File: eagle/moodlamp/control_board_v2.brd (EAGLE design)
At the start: 49.5 x 43.2 mm, 38 parts, among them IC1 MEGA8-AI, J1 POWER_JACKPTH, Q1 N-HEXFET-2D_SOT232-IRLL014N, Q2 N-HEXFET-2D_SOT232-IRLL014N, Q3 N-HEXFET-2D_SOT232-IRLL014N

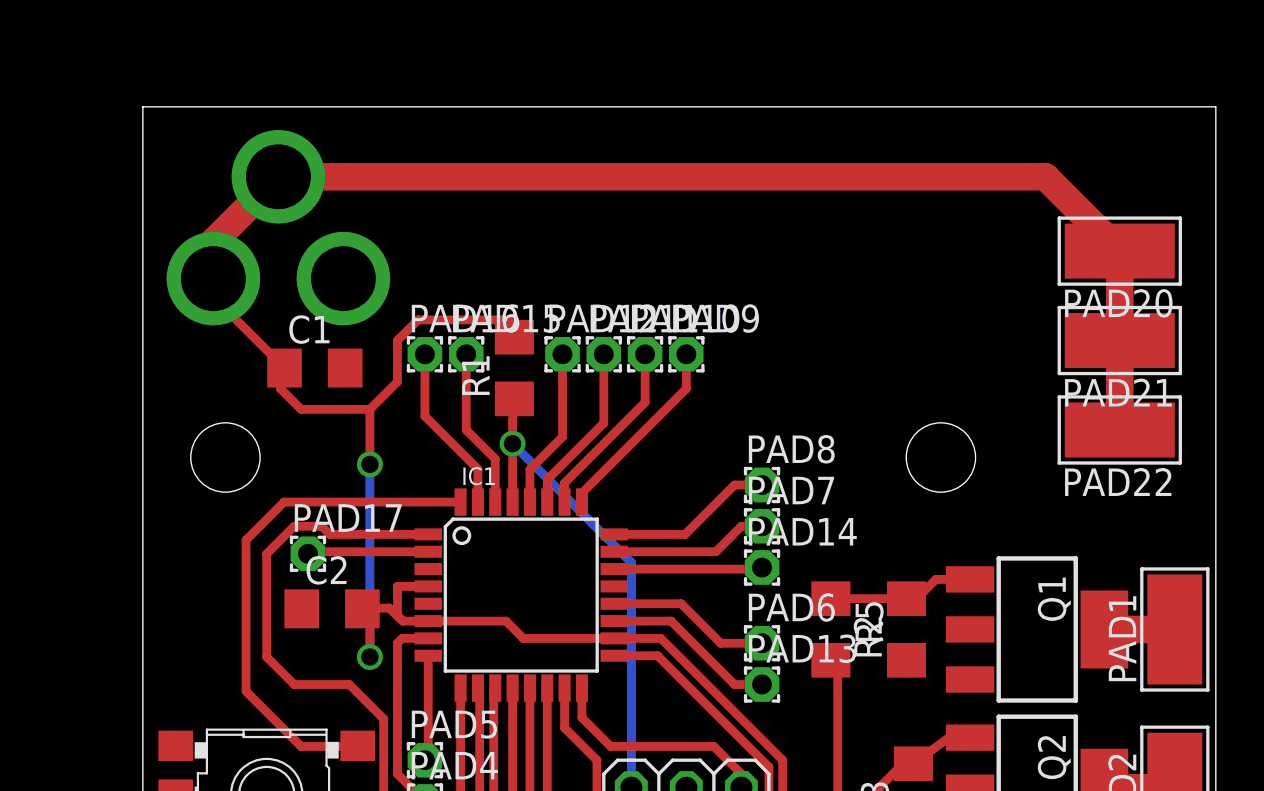
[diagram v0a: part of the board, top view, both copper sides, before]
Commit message: power jack fixed
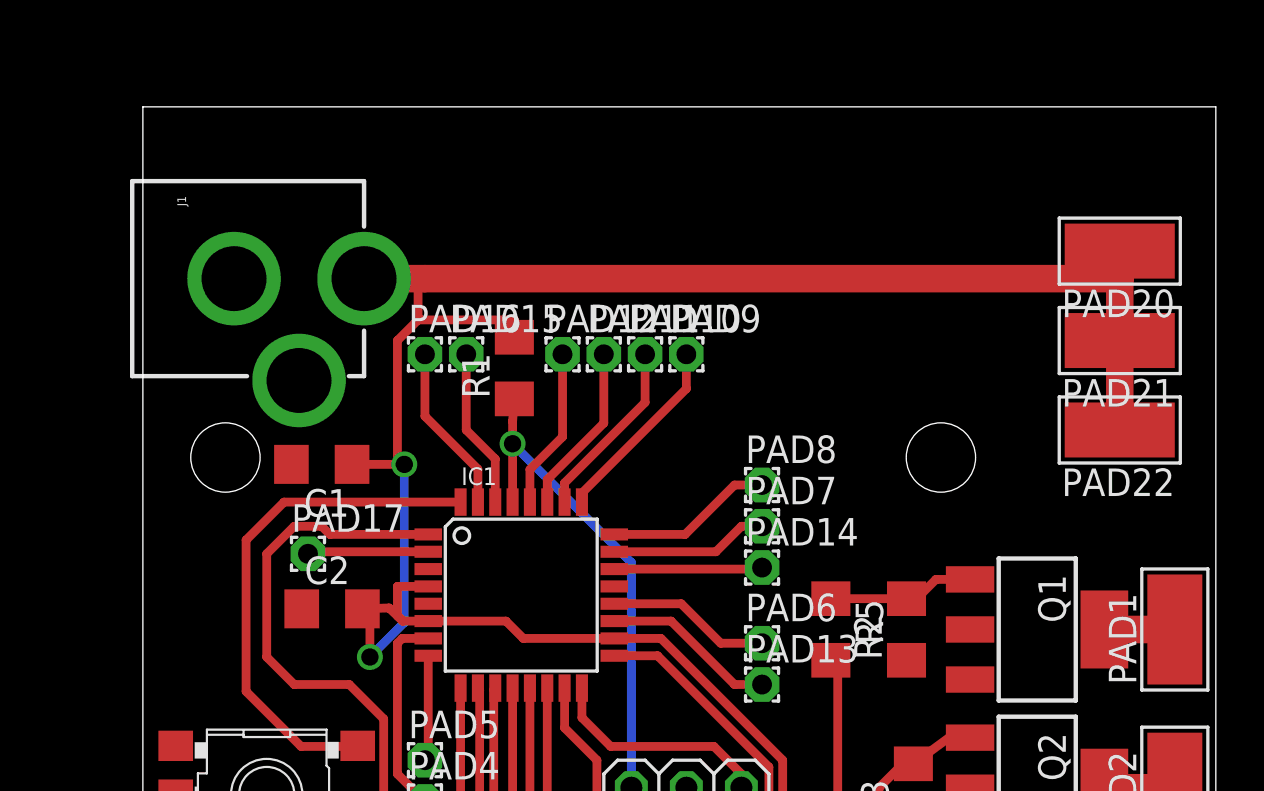
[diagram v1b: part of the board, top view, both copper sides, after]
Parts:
- moved C1 4.46 mm to (8.26, 26.7), turned to 180 degrees
- moved J1 0.95 mm to (-3.49, 35.2), flipped to the top, turned to 270 degrees
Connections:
- net GND: now also J1.GND, J1.GNDBREAK; no longer J1.PWR
- net VCC: now also J1.PWR; no longer J1.GND, J1.GNDBREAK
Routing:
- net VCC: track 120.0 -> 102.5 mm
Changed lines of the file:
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@@
 <attribute name="OC_FARNELL" value="9171371" x="47.9425" y="15.5575" size="1.778" layer="27" display="off"/>
 </element>
-<element name="J1" library="SparkFun" package="POWER_JACK_PTH" value="POWER_JACKPTH" x="-4.445" y="35.2425" rot="MR90"/>
-<element name="C1" library="resistor" package="C1206" value="" x="7.9375" y="31.115"/>
+<element name="J1" library="SparkFun" package="POWER_JACK_PTH" value="POWER_JACKPTH" x="-3.4925" y="35.2425" rot="R270"/>
+<element name="C1" library="resistor" package="C1206" value="" x="8.255" y="26.67" rot="R180"/>
 <element name="C2" library="resistor" package="C1206" value="" x="8.73125" y="20.0025"/>
 <element name="R1" library="resistor" package="R1206" value="" x="17.145" y="31.115" rot="R90"/>
@@
 <contactref element="IC1" pad="5"/>
 <contactref element="C1" pad="2"/>
-<contactref element="J1" pad="PWR"/>
 <contactref element="IC1" pad="21"/>
 <contactref element="Q1" pad="3"/>
@@
 <contactref element="USB1" pad="GND3"/>
 <contactref element="USB1" pad="GND4"/>
+<contactref element="J1" pad="GND"/>
+<contactref element="J1" pad="GNDBREAK"/>
 </signal>
 <signal name="VCC">
@@
 <contactref element="IC1" pad="4"/>
 <contactref element="C1" pad="1"/>
-<contactref element="J1" pad="GND"/>
-<contactref element="J1" pad="GNDBREAK"/>
 <contactref element="IC1" pad="18"/>
 <contactref element="R1" pad="2"/>
@@
 <contactref element="PAD21" pad="1"/>
 <contactref element="PAD22" pad="1"/>
-<wire x1="3.255" y1="35.2425" x2="3.255" y2="36.9425" width="1.27" layer="1"/>
-<wire x1="3.255" y1="36.9425" x2="6.255" y2="39.9425" width="1.27" layer="1"/>
-<wire x1="45.085" y1="36.5125" x2="41.655" y2="39.9425" width="1.27" layer="1"/>
-<wire x1="41.655" y1="39.9425" x2="6.255" y2="39.9425" width="1.27" layer="1"/>
-<wire x1="45.085" y1="36.5125" x2="45.085" y2="32.385" width="1.27" layer="1"/>
+<wire x1="45.085" y1="36.5125" x2="45.085" y2="35.2425" width="1.27" layer="1"/>
+<wire x1="45.085" y1="35.2425" x2="45.085" y2="32.385" width="1.27" layer="1"/>
 <wire x1="45.085" y1="32.385" x2="45.085" y2="28.2575" width="1.27" layer="1"/>
-<wire x1="3.255" y1="35.2425" x2="3.255" y2="34.3975" width="0.4064" layer="1"/>
-<wire x1="3.255" y1="34.3975" x2="6.5375" y2="31.115" width="0.4064" layer="1"/>
 <wire x1="21.7551" y1="18.6375" x2="17.5575" y2="18.6375" width="0.4064" layer="1"/>
 <wire x1="17.5575" y1="18.6375" x2="16.7575" y2="19.4375" width="0.4064" layer="1"/>
@@
 <wire x1="17.145" y1="33.3375" x2="12.7" y2="33.3375" width="0.4064" layer="1"/>
 <wire x1="12.7" y1="33.3375" x2="11.7475" y2="32.385" width="0.4064" layer="1"/>
-<wire x1="11.7475" y1="32.385" x2="11.7475" y2="30.48" width="0.4064" layer="1"/>
-<wire x1="10.4775" y1="29.21" x2="7.3025" y2="29.21" width="0.4064" layer="1"/>
-<wire x1="7.3025" y1="29.21" x2="6.35" y2="30.1625" width="0.4064" layer="1"/>
-<wire x1="6.35" y1="30.1625" x2="6.35" y2="30.9275" width="0.4064" layer="1"/>
-<wire x1="6.35" y1="30.9275" x2="6.5375" y2="31.115" width="0.4064" layer="1"/>
-<wire x1="10.4775" y1="29.21" x2="11.7475" y2="30.48" width="0.4064" layer="1"/>
-<wire x1="10.4775" y1="29.21" x2="10.4775" y2="26.67" width="0.4064" layer="1"/>
-<via x="10.4775" y="26.67" extent="1-16" drill="0.8"/>
-<wire x1="10.4775" y1="26.67" x2="10.4775" y2="17.78" width="0.4064" layer="16"/>
+<wire x1="11.7475" y1="32.385" x2="11.7475" y2="26.9875" width="0.4064" layer="1"/>
+<wire x1="11.7475" y1="26.9875" x2="12.065" y2="26.67" width="0.4064" layer="1"/>
+<via x="12.065" y="26.67" extent="1-16" drill="0.8"/>
+<wire x1="12.065" y1="26.67" x2="12.065" y2="19.3675" width="0.4064" layer="16"/>
+<wire x1="12.065" y1="19.3675" x2="10.4775" y2="17.78" width="0.4064" layer="16"/>
 <via x="10.4775" y="17.78" extent="1-16" drill="0.8"/>
 <wire x1="10.4775" y1="17.78" x2="10.4775" y2="19.65625" width="0.4064" layer="1"/>
 <wire x1="10.4775" y1="19.65625" x2="10.13125" y2="20.0025" width="0.4064" layer="1"/>
+<contactref element="J1" pad="PWR"/>
+<wire x1="10.2075" y1="35.2425" x2="13.0175" y2="35.2425" width="1.27" layer="1"/>
+<wire x1="13.0175" y1="35.2425" x2="45.085" y2="35.2425" width="1.27" layer="1"/>
+<wire x1="9.655" y1="26.67" x2="12.065" y2="26.67" width="0.4064" layer="1"/>
+<wire x1="12.7" y1="33.3375" x2="12.7" y2="35.2425" width="0.4064" layer="1"/>
+<wire x1="12.7" y1="35.2425" x2="13.0175" y2="35.2425" width="0.4064" layer="1"/>
 </signal>
 <signal name="RST">

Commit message: v2 prototype
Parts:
- added D1, D2: 3V6, diode:SOD80C
- added R6: 1k5, resistor:R0805
- added R7, R8: 68R, resistor:R0805
- C1, C2: device resistor:C1206 -> resistor:C0805
- PAD1, PAD2, PAD20, PAD21, PAD22, PAD3: value WIREPADSMD5-2,5 -> (none); device wirepad:5-2,5 -> wirepad:2,54/1,0
- R1, R2, R3, R4, R5: device resistor:R1206 -> resistor:R0805
- moved USB1 26.2 mm to (1.27, 23.2), turned to 0 degrees
- moved PAD17 20.5 mm to (18.4, 5.08)
- moved C1 11.8 mm to (15.6, 35.9), turned to 90 degrees
- moved PAD16 9.34 mm to (11.4, 22.5)
- moved PAD19 3.82 mm to (20.3, 5.08)
- moved C2 3.18 mm to (11.9, 20.0)
- moved PAD15 3.18 mm to (17.5, 29.8)
- moved JP1 2.88 mm to (27.9, 10.8)
- moved PAD10 2.69 mm to (25.1, 29.8)
- moved PAD12 2.69 mm to (21.3, 29.8)
- moved PAD9 2.69 mm to (27.0, 29.8)
- moved PAD11 2.69 mm to (23.2, 29.8)
- moved PAD4 2.62 mm to (15.6, 10.5)
- moved PAD5 2.62 mm to (15.6, 12.4)
- moved R1 2.56 mm to (19.4, 32.4)
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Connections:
- new net N$30: D1.C, R6.2, R7.2, USB1.2
- new net N$31: D2.C, R8.2, USB1.3
- net +5V: now also R6.1
- net GND: now also D1.A, D2.A
- net N$10: now also IC1.31, R7.1; no longer IC1.10, USB1.2
- net N$11: now also IC1.32, R8.1; no longer IC1.11, USB1.3
- net N$24: now also IC1.2; no longer IC1.31
- net N$25: now also IC1.11; no longer IC1.2
- net N$8: now also IC1.10, S2.3; no longer IC1.32, S1.3
- net N$9: now also S1.3; no longer S2.3
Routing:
- net N$30: track 0.00 -> 17.8 mm
- net N$9: track 28.7 -> 15.5 mm
- net N$10: track 12.0 -> 2.96 mm
- net VCC: track 102.5 -> 111.3 mm, vias 2 -> 0
- net +5V: track 0.00 -> 8.41 mm
- net N$31: track 0.00 -> 7.71 mm
- net N$11: track 12.0 -> 4.35 mm
- net N$8: track 23.8 -> 16.5 mm
- net GND: track 0.00 -> 6.30 mm, vias 0 -> 2
- net N$25: track 5.59 -> 11.3 mm
- net N$27: track 16.5 -> 11.7 mm
- net RST: track 22.9 -> 27.0 mm
- net N$24: track 7.83 -> 4.00 mm
- net N$12: track 7.50 -> 5.24 mm
- net N$6: track 31.4 -> 29.2 mm
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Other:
- board size 49.5 x 43.2 mm -> 49.5 x 40 mm
- board text added: "moodlamp v2"

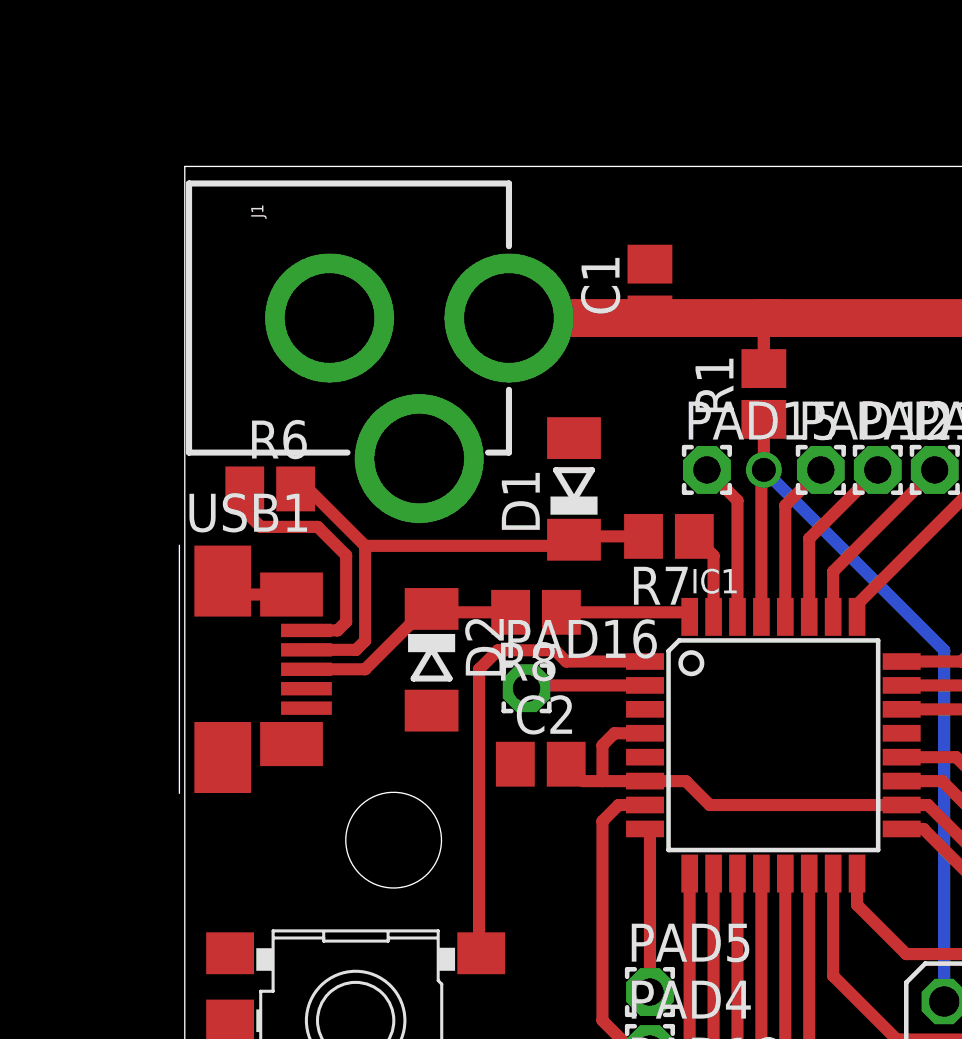
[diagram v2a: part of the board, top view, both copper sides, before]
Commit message: power jack orientation fixed
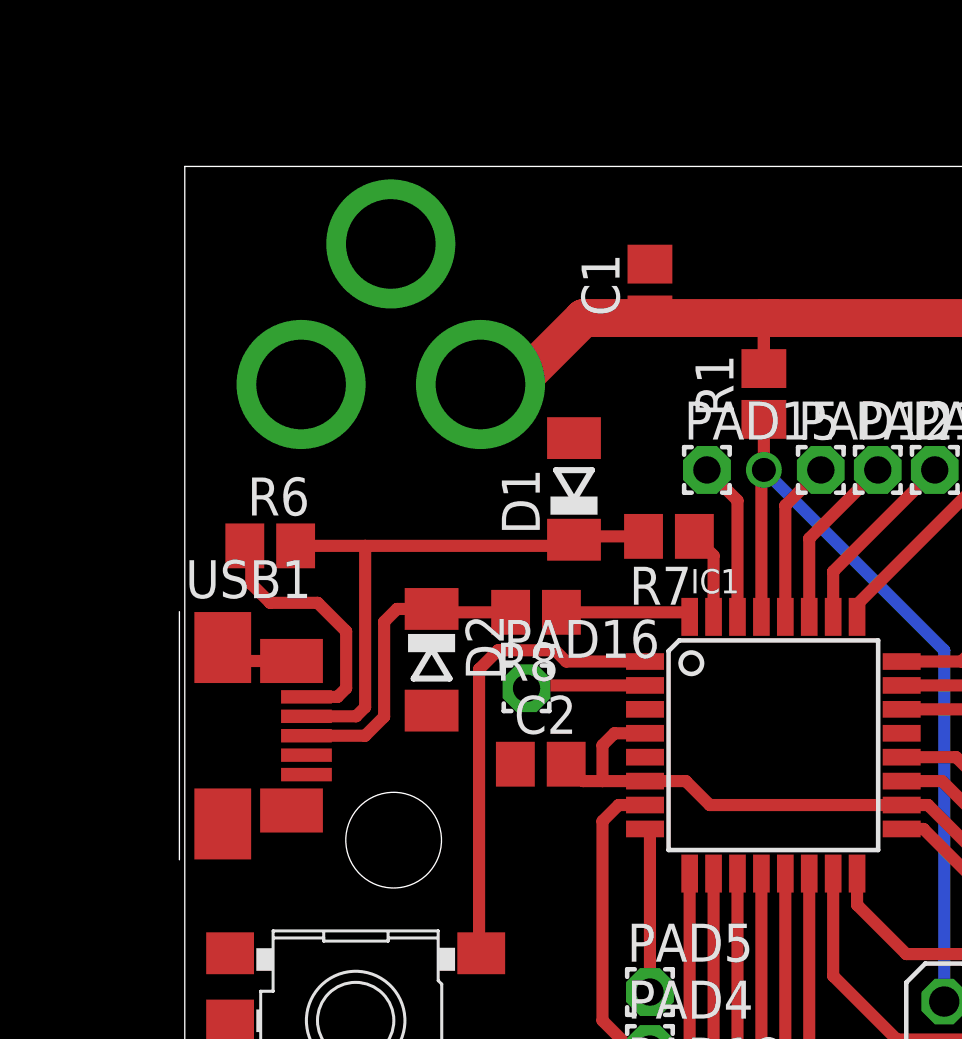
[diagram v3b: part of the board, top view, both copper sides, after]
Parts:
- moved J1 2.42 mm to (-3.81, 32.7), flipped to the bottom, turned to 90 degrees
- moved USB1 2.22 mm to (1.27, 21.0)
- moved R6 1.91 mm to (2.86, 27.3)
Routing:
- net N$31: track 7.71 -> 10.7 mm
- net VCC: track 111.3 -> 113.6 mm
- net N$30: track 17.8 -> 19.3 mm
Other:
- board text added: "tohle je moc blizko u sebe ->"
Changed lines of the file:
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@@
 <hole x="38.735" y="28.2575" drill="3.2"/>
 <text x="33.02" y="32.0675" size="1.016" layer="1" font="vector">moodlamp v2</text>
+<text x="-17.145" y="28.575" size="0.6096" layer="48">tohle je moc blizko u sebe -&gt;</text>
 </plain>
 <attributes>
@@
 <attribute name="OC_FARNELL" value="9171371" x="50.165" y="15.5575" size="1.778" layer="27" display="off"/>
 </element>
-<element name="J1" library="SparkFun" package="POWER_JACK_PTH" value="POWER_JACKPTH" x="-2.8575" y="34.925" rot="R270"/>
+<element name="J1" library="SparkFun" package="POWER_JACK_PTH" value="POWER_JACKPTH" x="-3.81" y="32.7025" rot="MR90"/>
 <element name="C1" library="resistor" package="C0805" value="" x="15.5575" y="35.8775" rot="R90"/>
 <element name="C2" library="resistor" package="C0805" value="" x="11.90625" y="20.0025"/>
@@
 <element name="S1" library="switch" package="SKHMPXE010" value="SKHMPSE010" x="5.715" y="11.43" rot="R180"/>
 <element name="S2" library="switch" package="SKHMPXE010" value="SKHMPSE010" x="5.715" y="4.1275" rot="R180"/>
-<element name="USB1" library="usb_con-update" package="MOLEX-47364-0001" value="MOLEX-47346-0001" x="1.27" y="23.1775"/>
+<element name="USB1" library="usb_con-update" package="MOLEX-47364-0001" value="MOLEX-47346-0001" x="1.27" y="20.955"/>
 <element name="JP1" library="pinhead" package="2X03" value="" x="27.94" y="10.795" rot="R180"/>
 <element name="PAD4" library="wirepad" package="1,6/0,9" value="" x="15.5575" y="10.4775"/>
@@
 <element name="PAD17" library="wirepad" package="1,6/0,9" value="" x="18.415" y="5.08"/>
 <element name="PAD16" library="wirepad" package="1,6/0,9" value="" x="11.43" y="22.5425"/>
-<element name="R6" library="resistor" package="R0805" value="1k5" x="2.8575" y="29.21"/>
+<element name="R6" library="resistor" package="R0805" value="1k5" x="2.8575" y="27.305"/>
 <element name="R7" library="resistor" package="R0805" value="68R" x="16.1925" y="27.6225" rot="R180"/>
 <element name="R8" library="resistor" package="R0805" value="68R" x="11.7475" y="25.0825" rot="R180"/>
@@
 <contactref element="D1" pad="A"/>
 <contactref element="D2" pad="A"/>
-<wire x1="3.57" y1="25.6775" x2="1.72" y2="25.6775" width="0.4064" layer="1"/>
-<wire x1="1.72" y1="25.6775" x2="1.27" y2="26.1275" width="0.4064" layer="1"/>
+<wire x1="3.57" y1="23.455" x2="1.72" y2="23.455" width="0.4064" layer="1"/>
+<wire x1="1.72" y1="23.455" x2="1.27" y2="23.905" width="0.4064" layer="1"/>
 <via x="28.8925" y="33.02" extent="1-16" drill="0.8"/>
 <via x="28.8925" y="36.83" extent="1-16" drill="0.8"/>
@@
 <wire x1="15.3924" y1="19.4375" x2="16.7575" y2="19.4375" width="0.4064" layer="1"/>
 <contactref element="J1" pad="PWR"/>
-<wire x1="10.8425" y1="34.925" x2="15.875" y2="34.925" width="1.27" layer="1"/>
-<wire x1="15.875" y1="34.925" x2="19.3675" y2="34.925" width="1.27" layer="1"/>
+<wire x1="16.09" y1="34.925" x2="19.3675" y2="34.925" width="1.27" layer="1"/>
 <wire x1="19.3675" y1="34.925" x2="19.685" y2="34.925" width="1.27" layer="1"/>
 <wire x1="19.685" y1="34.925" x2="32.0675" y2="34.925" width="1.27" layer="1"/>
@@
 <wire x1="13.32125" y1="19.4375" x2="12.75625" y2="20.0025" width="0.4064" layer="1"/>
 <wire x1="15.5575" y1="35.0275" x2="15.7725" y2="35.0275" width="0.4064" layer="1"/>
-<wire x1="15.7725" y1="35.0275" x2="15.875" y2="34.925" width="0.4064" layer="1"/>
 <wire x1="19.3675" y1="33.235" x2="19.3675" y2="34.6075" width="0.4064" layer="1"/>
 <wire x1="19.3675" y1="34.6075" x2="19.685" y2="34.925" width="0.4064" layer="1"/>
@@
 <wire x1="31.75" y1="34.6075" x2="31.75" y2="14.605" width="0.4064" layer="1"/>
 <wire x1="31.75" y1="14.605" x2="31.115" y2="13.97" width="0.4064" layer="1"/>
+<wire x1="13.335" y1="34.925" x2="11.1125" y2="32.7025" width="1.27" layer="1"/>
+<wire x1="11.1125" y1="32.7025" x2="9.89" y2="32.7025" width="1.27" layer="1"/>
+<wire x1="15.5575" y1="35.0275" x2="16.09" y2="34.925" width="1.27" layer="1"/>
+<wire x1="16.09" y1="34.925" x2="13.335" y2="34.925" width="1.27" layer="1"/>
 </signal>
 <signal name="RST">
@@
 <contactref element="USB1" pad="1"/>
 <contactref element="R6" pad="1"/>
-<wire x1="4.07" y1="24.4775" x2="5.11" y2="24.4775" width="0.4064" layer="1"/>
-<wire x1="5.11" y1="24.4775" x2="5.3975" y2="24.765" width="0.4064" layer="1"/>
-<wire x1="5.3975" y1="24.765" x2="5.3975" y2="26.9875" width="0.4064" layer="1"/>
-<wire x1="5.3975" y1="26.9875" x2="4.445" y2="27.94" width="0.4064" layer="1"/>
-<wire x1="4.445" y1="27.94" x2="2.54" y2="27.94" width="0.4064" layer="1"/>
-<wire x1="2.0075" y1="29.21" x2="2.0075" y2="28.4725" width="0.4064" layer="1"/>
-<wire x1="2.0075" y1="28.4725" x2="2.54" y2="27.94" width="0.4064" layer="1"/>
+<wire x1="4.07" y1="22.255" x2="5.11" y2="22.255" width="0.4064" layer="1"/>
+<wire x1="5.11" y1="22.255" x2="5.3975" y2="22.5425" width="0.4064" layer="1"/>
+<wire x1="2.0075" y1="27.305" x2="2.2225" y2="27.09" width="0.4064" layer="1"/>
+<wire x1="2.2225" y1="27.09" x2="2.2225" y2="26.035" width="0.4064" layer="1"/>
+<wire x1="2.2225" y1="26.035" x2="2.8575" y2="25.4" width="0.4064" layer="1"/>
+<wire x1="2.8575" y1="25.4" x2="4.445" y2="25.4" width="0.4064" layer="1"/>
+<wire x1="4.445" y1="25.4" x2="5.3975" y2="24.4475" width="0.4064" layer="1"/>
+<wire x1="5.3975" y1="24.4475" x2="5.3975" y2="22.5425" width="0.4064" layer="1"/>
 </signal>
 <signal name="N$12">
@@
 <wire x1="15.3425" y1="27.6225" x2="13.13" y2="27.6225" width="0.4064" layer="1"/>
 <wire x1="13.13" y1="27.6225" x2="13.0175" y2="27.51" width="0.4064" layer="1"/>
-<wire x1="3.7075" y1="29.21" x2="4.1275" y2="29.21" width="0.4064" layer="1"/>
-<wire x1="4.1275" y1="29.21" x2="6.0325" y2="27.305" width="0.4064" layer="1"/>
 <wire x1="6.0325" y1="27.305" x2="12.8125" y2="27.305" width="0.4064" layer="1"/>
 <wire x1="12.8125" y1="27.305" x2="13.0175" y2="27.51" width="0.4064" layer="1"/>
-<wire x1="4.07" y1="23.8275" x2="5.73" y2="23.8275" width="0.4064" layer="1"/>
-<wire x1="5.73" y1="23.8275" x2="6.0325" y2="24.13" width="0.4064" layer="1"/>
-<wire x1="6.0325" y1="24.13" x2="6.0325" y2="27.305" width="0.4064" layer="1"/>
+<wire x1="4.07" y1="21.605" x2="5.73" y2="21.605" width="0.4064" layer="1"/>
+<wire x1="5.73" y1="21.605" x2="6.0325" y2="21.9075" width="0.4064" layer="1"/>
+<wire x1="6.0325" y1="21.9075" x2="6.0325" y2="27.305" width="0.4064" layer="1"/>
+<wire x1="3.7075" y1="27.305" x2="6.0325" y2="27.305" width="0.4064" layer="1"/>
 </signal>
 <signal name="N$31">
@@
 <wire x1="8.3675" y1="25.0825" x2="8.255" y2="25.195" width="0.4064" layer="1"/>
 <wire x1="8.255" y1="25.195" x2="8.05" y2="25.195" width="0.4064" layer="1"/>
-<wire x1="8.05" y1="25.195" x2="6.0325" y2="23.1775" width="0.4064" layer="1"/>
-<wire x1="6.0325" y1="23.1775" x2="4.07" y2="23.1775" width="0.4064" layer="1"/>
+<wire x1="6.0325" y1="20.955" x2="4.07" y2="20.955" width="0.4064" layer="1"/>
+<wire x1="6.0325" y1="20.955" x2="6.6675" y2="21.59" width="0.4064" layer="1"/>
+<wire x1="6.6675" y1="21.59" x2="6.6675" y2="24.765" width="0.4064" layer="1"/>
+<wire x1="6.6675" y1="24.765" x2="7.0975" y2="25.195" width="0.4064" layer="1"/>
+<wire x1="7.0975" y1="25.195" x2="8.255" y2="25.195" width="0.4064" layer="1"/>
 </signal>
 </signals>
